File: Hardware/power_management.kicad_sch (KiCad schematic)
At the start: 36 parts, among them J2 Conn_01x03, SW97 Power_switch, U2 BQ24040, U3 BQ51050BRHL, U4 AP22814BW5

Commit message: Completed Final GUI Key Layout and PCB key layout draft
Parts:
- U2: footprint (none) -> Package_DFN_QFN:Texas_DLH0010A_WSON-10-1EP_2.2x2mm_P0.4mm_EP0.9x1.5mm_ThermalVias
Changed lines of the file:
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@@
 			)
 		)
-		(property "Footprint" ""
+		(property "Footprint" "Package_DFN_QFN:Texas_DLH0010A_WSON-10-1EP_2.2x2mm_P0.4mm_EP0.9x1.5mm_ThermalVias"
 			(at 118.11 66.04 0)
 			(effects

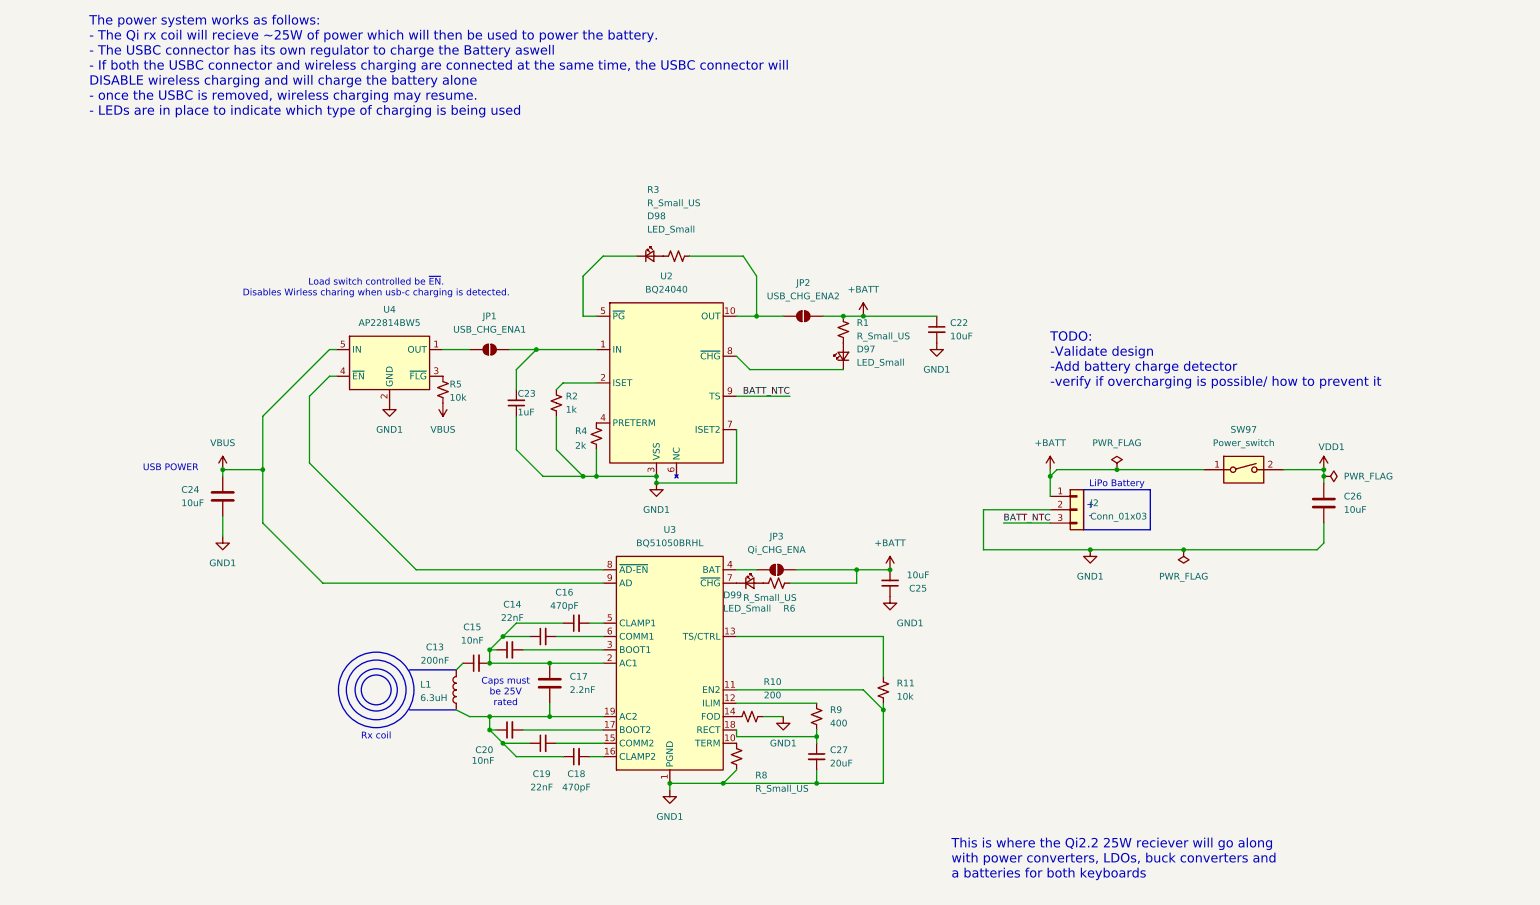
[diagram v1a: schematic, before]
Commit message: Update footprints and switch symbol in schematic
Set proper SMD footprints for capacitors, resistors, inductors, crystals, and net ties in hornet_kb.kicad_sch. In power_management.kicad_sch, replace DIP switch symbol with DPDT switch, update related symbol properties, add new switch instance, and adjust wiring and annotation for improved clarity and functionality. Man i love summarize with copilot
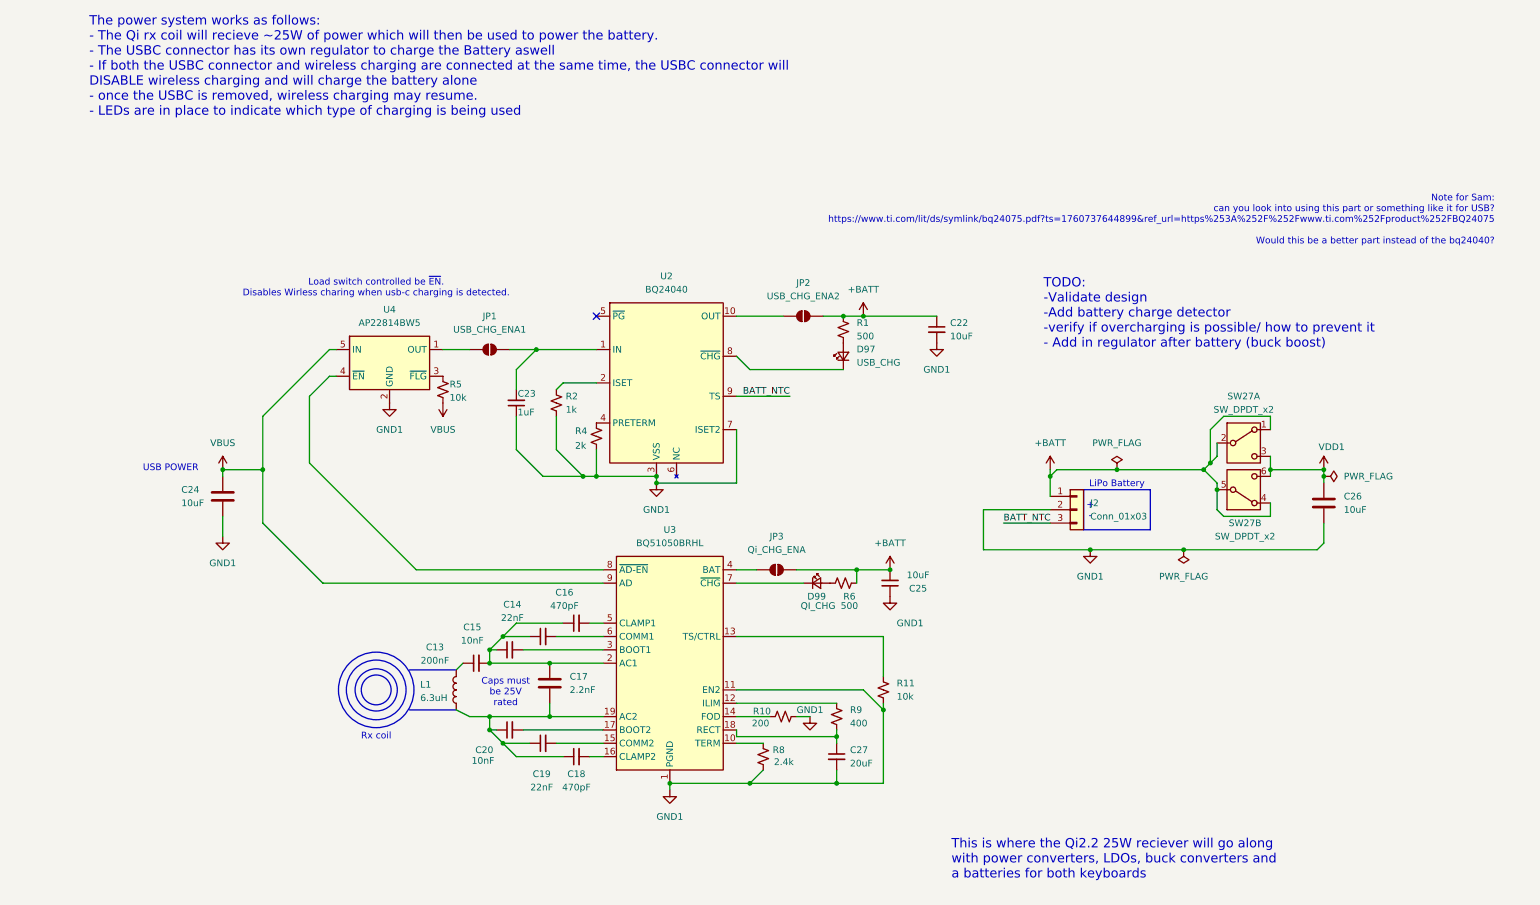
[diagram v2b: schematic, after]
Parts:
- removed D98: LED_Small, symbol Device:LED_Small
- removed R3: R_Small_US, symbol Device:R_Small_US
- removed SW97: Power_switch, symbol Switch:SW_DIP_x01
- added SW27: SW_DPDT_x2, symbol Switch:SW_DPDT_x2
- C13, C14, C15, C16, C17, C18, C19, C20, C22, C23, C24, C25, C26, C27: footprint (none) -> Capacitor_SMD:C_0603_1608Metric
- D97: value LED_Small -> USB_CHG; footprint (none) -> LED_SMD:LED_0402_1005Metric
- D99: value LED_Small -> QI_CHG
- J2: footprint (none) -> Connector_JST:JST_GH_SM02B-GHS-TB_1x02-1MP_P1.25mm_Horizontal
- L1: footprint (none) -> Connector_JST:JST_EH_S2B-EH_1x02_P2.50mm_Horizontal
- R1, R6: value R_Small_US -> 500; footprint (none) -> Resistor_SMD:R_0603_1608Metric
- R10, R11, R2, R4, R5, R9: footprint (none) -> Resistor_SMD:R_0603_1608Metric
- R8: value R_Small_US -> 2.4k; footprint (none) -> Resistor_SMD:R_0603_1608Metric
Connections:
- net +BATT: now also SW27.1 (A), SW27.2 (B), SW27.4 (A), SW27.5 (B)
- net VDD1: now also SW27.3 (C), SW27.6 (C)
- no-connect marks 0 -> 1
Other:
- note added: "Note for Sam: can you look into using this part or something like it for USB? https://www.ti.com/lit/ds/symlink/bq24075.pdf?ts=1760737644899&ref_url=https%253A%252F%252Fwww.ti.com%252Fproduct%252FBQ24075 Would this be a better part instead of the bq24040?"
- note added: "TODO: -Validate design -Add battery charge detector -verify if overcharging is possible/ how to prevent it - Add in regulator after battery (buck boost)"
- note removed: "TODO: -Validate design -Add battery charge detector -verify if overcharging is possible/ how to prevent it"
- moved on the sheet: C27, D99, R10, R6, R8, R9

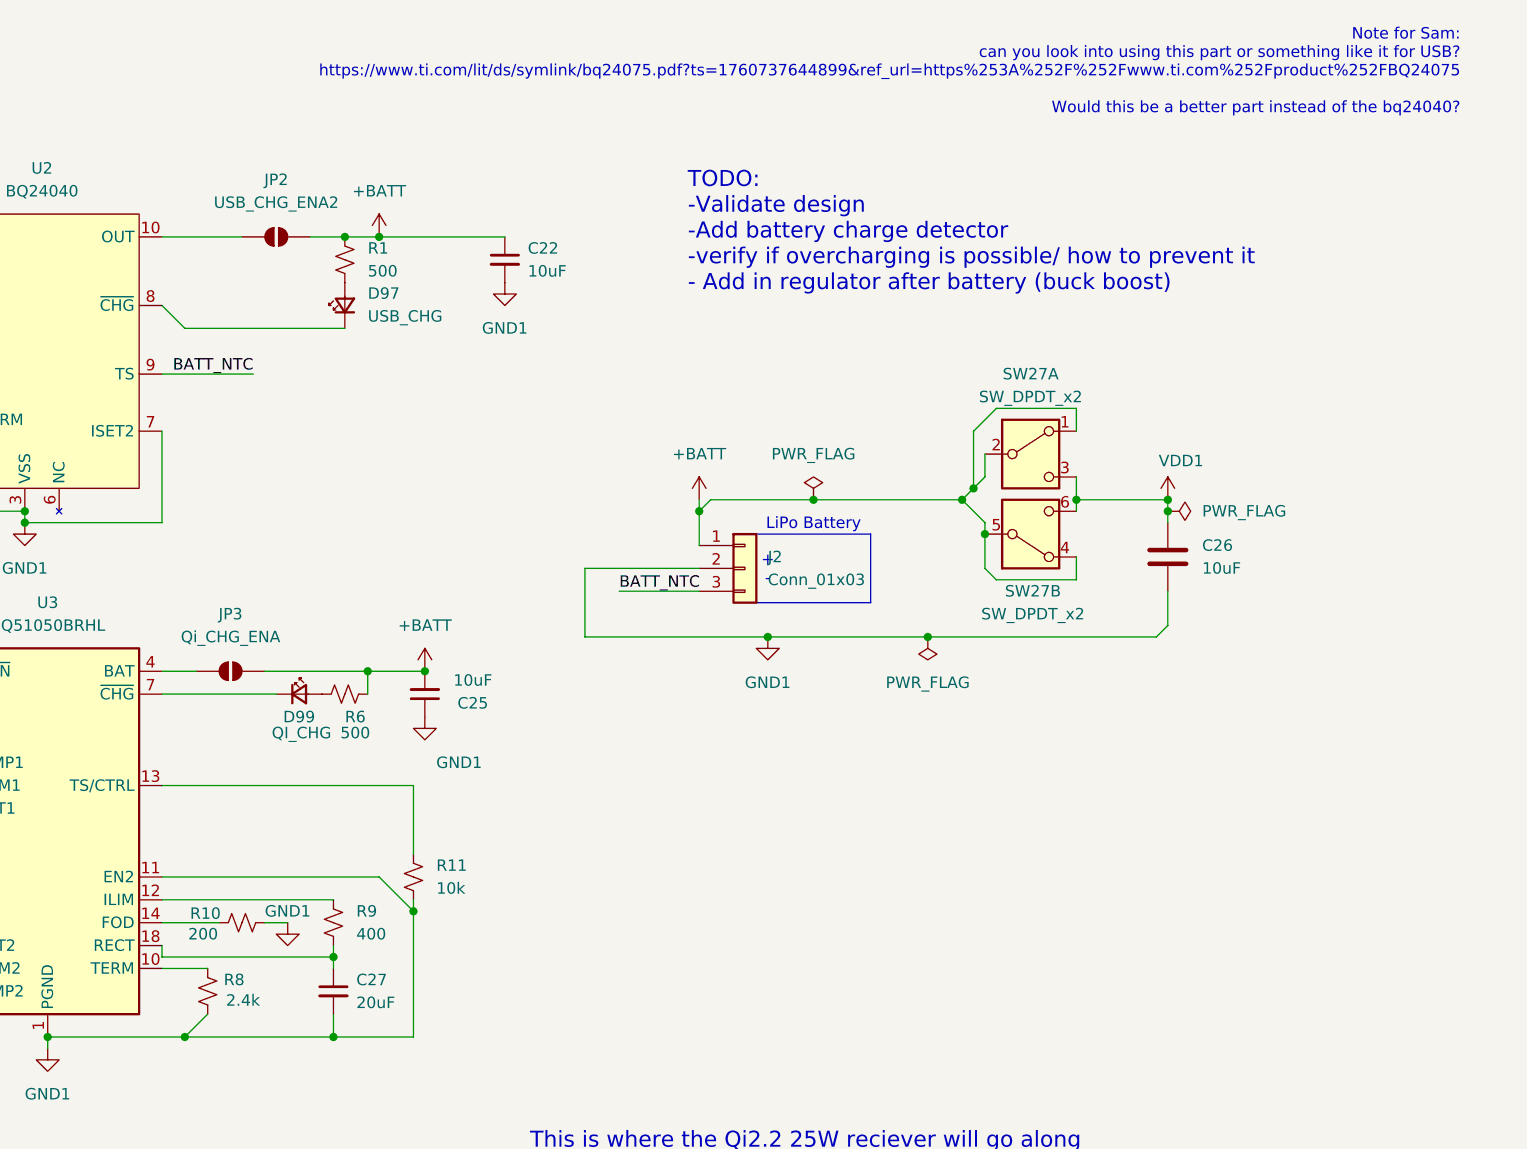
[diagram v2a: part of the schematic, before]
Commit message: Added LDO to battery and added placement for the charging modules
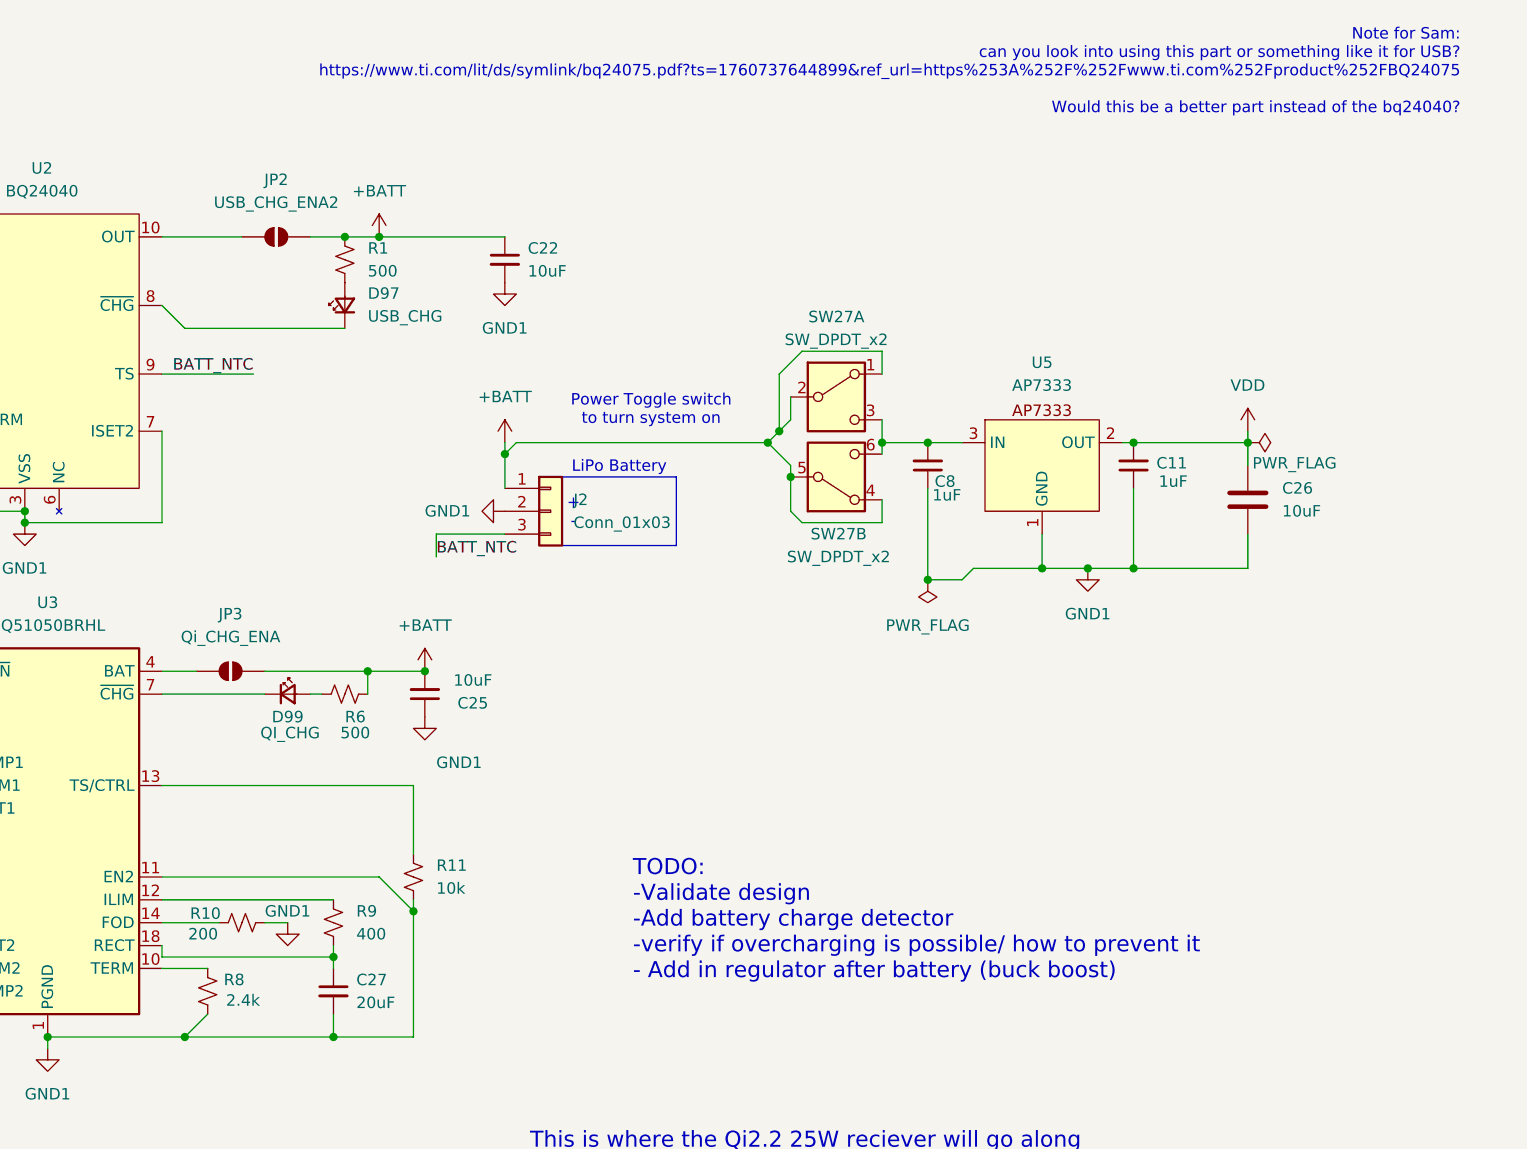
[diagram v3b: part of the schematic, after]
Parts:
- added C11, C8: 1uF, Capacitor_SMD:C_0603_1608Metric, symbol Device:C_Small
- added U5: AP7333, Package_TO_SOT_SMD:SOT-23, symbol Custom_sym:AP7333-33
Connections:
- net GND1: now also C11.1, C8.1, U5.1 (GND)
- net VDD1: no longer names the net of SW27.3 (C), SW27.6 (C)
- net VDD1: now also C8.2, U5.3 (IN); no longer C26.1
- new net VDD: C11.2, C26.1, U5.2 (OUT)
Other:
- note added: "Power Toggle switch to turn system on"
- moved on the sheet: C26, D99, J2, SW27A, SW27B
